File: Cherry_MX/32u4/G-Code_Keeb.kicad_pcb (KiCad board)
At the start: 2 copper layers, 158.7 x 133.3 mm, 46 parts, among them J1 Conn_01x04, SW1 SW_Push_45deg, SW10 SW_Push_45deg, SW11 SW_Push_45deg, SW12 SW_Push_45deg, SW13 SW_Push_45deg, SW14 SW_Push_45deg, SW15 SW_Push_45deg, SW16 SW_Push_45deg, SW17 SW_Push_45deg, SW18 SW_Push_45deg, SW19 SW_Push_45deg, SW2 SW_Push_45deg, SW20 SW_Push_45deg, SW21 SW_Push_45deg, SW22 SW_Push_45deg, SW23 SW_Push_45deg, SW24 SW_Push, SW25 SW_Push, SW3 SW_Push_45deg, SW4 SW_Push_45deg, SW5 SW_Push_45deg, SW6 SW_Push_45deg, SW7 SW_Push_45deg, SW8 SW_Push_45deg, SW9 SW_Push_45deg, U1 ATmega32U4-A, Y1 16MHz

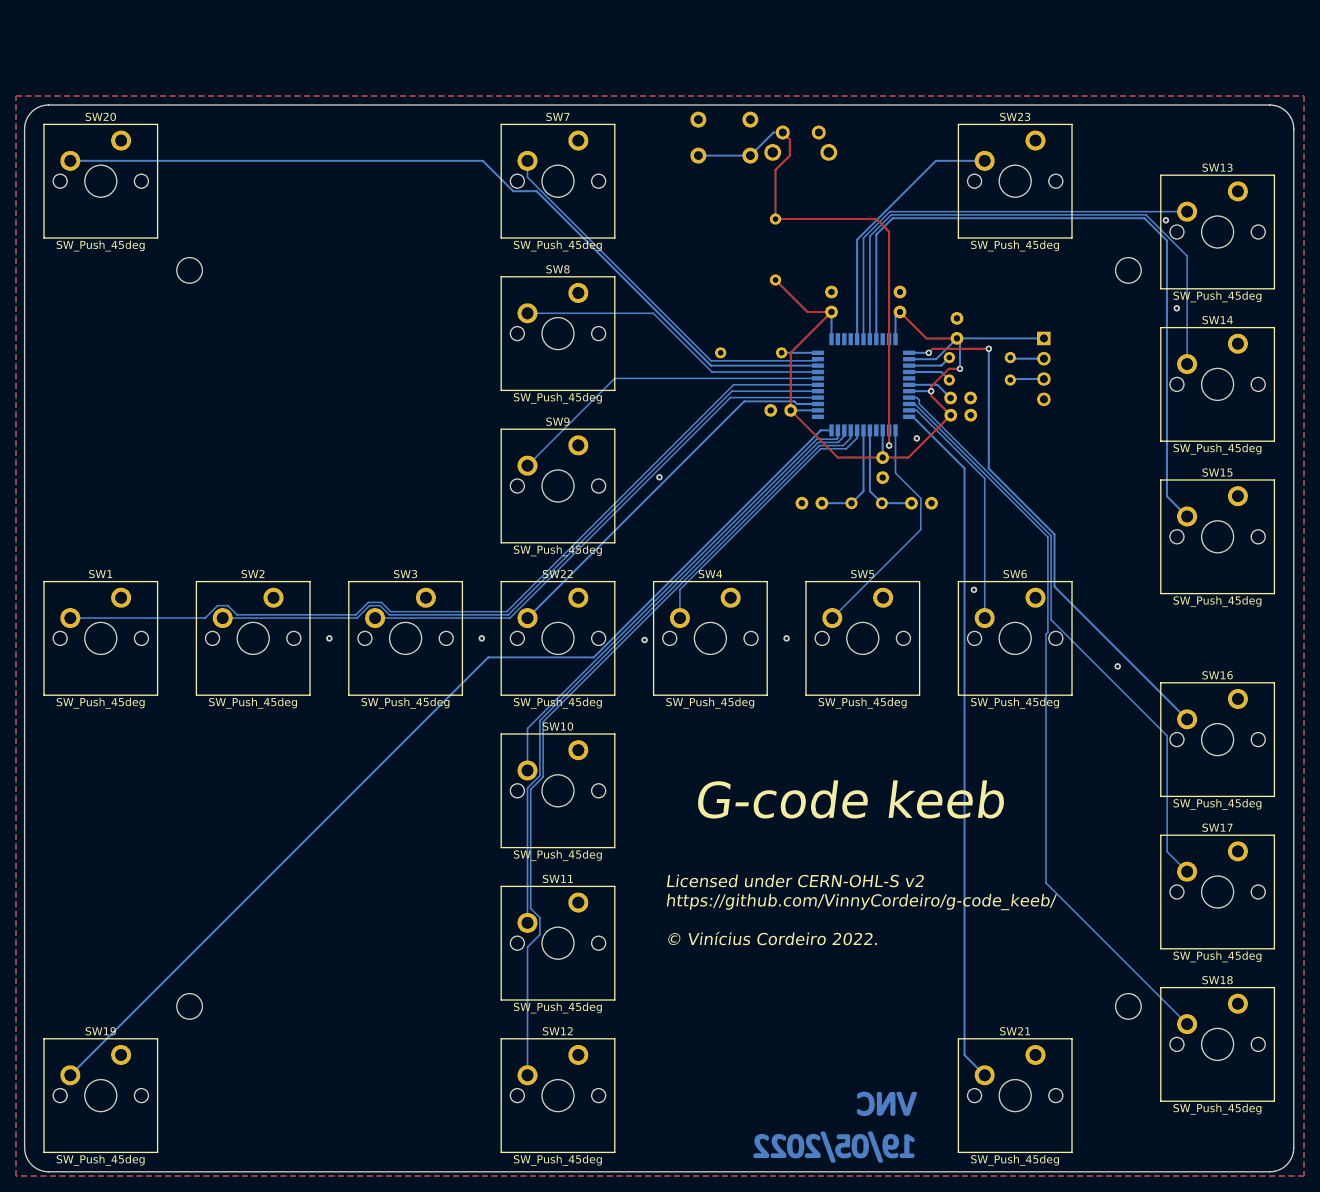
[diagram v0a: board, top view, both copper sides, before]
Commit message: Fixed mistake on X axis
The X axis values were mirrored, this commit fix that. That also includes the silkscreen.
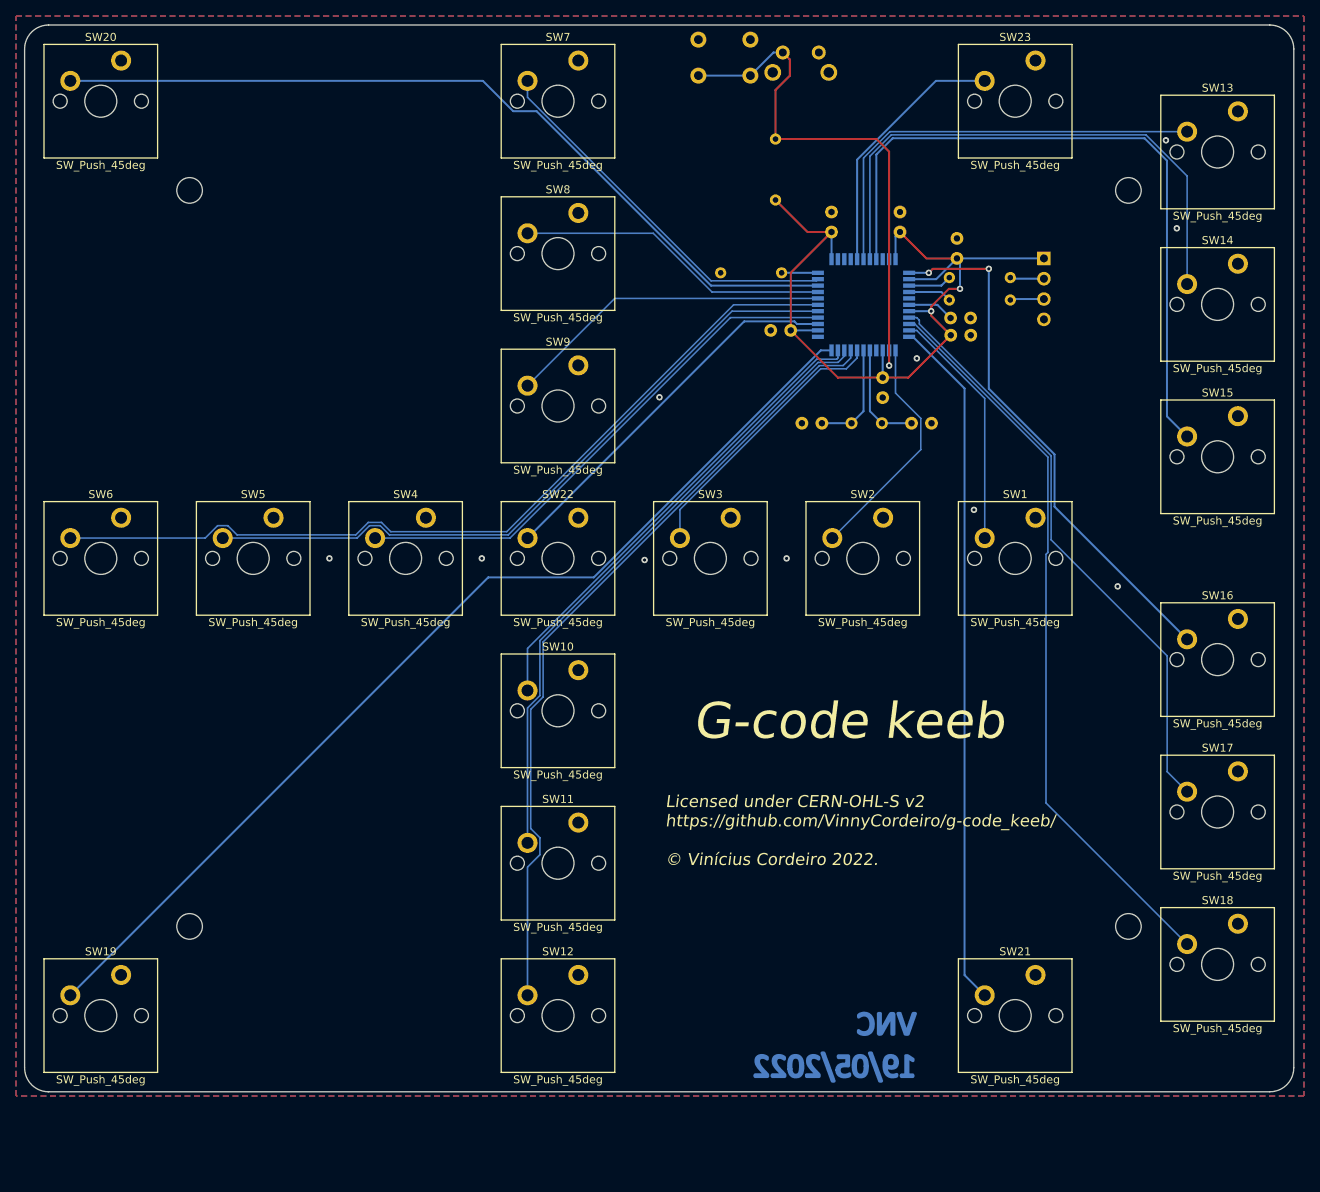
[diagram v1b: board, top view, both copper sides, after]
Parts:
- moved SW1 114.7 mm to (142.9, 94.8)
- moved SW6 114.7 mm to (28.6, 94.8)
- moved SW2 76.9 mm to (123.8, 94.8)
- moved SW5 76.9 mm to (47.6, 94.8)
- moved SW3 39.4 mm to (104.8, 94.8)
- moved SW4 39.4 mm to (66.7, 94.8)
- moved G*** 11.1 mm to (59.1, 94.8)
- moved SW25 10.0 mm to (109.8, 29.9)
- moved C1 10.0 mm to (132.4, 77.9)
- moved C2 10.0 mm to (118.7, 77.9)
- moved C3 10.0 mm to (137.3, 64.8)
- moved C4 10.0 mm to (135.6, 54.8)
- moved C5 10.0 mm to (137.3, 66.9)
- moved C6 10.0 mm to (126.3, 74.7)
- moved C7 10.0 mm to (112.3, 66.3)
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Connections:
- U1 pad 10: X-100 -> X+100
- U1 pad 12: X-10 -> X+10
- U1 pad 18: X-1 -> X+1
- U1 pad 26: X+1 -> X-1
- U1 pad 27: X+10 -> X-10
- U1 pad 28: X+100 -> X-100
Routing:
- net X+100: track 107.4 -> 30.4 mm
- net X-100: track 30.4 -> 107.4 mm
- net X-10: track 29.4 -> 87.1 mm
- net X+10: track 87.1 -> 29.4 mm
- net X-1: track 34.5 -> 66.8 mm
- net X+1: track 66.8 -> 34.5 mm

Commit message: Fixing the fix
Uploaded the wrong files, this commit corrects that.
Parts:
- SW1: value SW_Push_45deg -> Z+100
- SW10: value SW_Push_45deg -> Y-1
- SW11: value SW_Push_45deg -> Y-10
- SW12: value SW_Push_45deg -> Y-100
- SW13, SW2: value SW_Push_45deg -> Z+10
- SW14, SW3: value SW_Push_45deg -> Z+1
- SW15: value SW_Push_45deg -> Z+0.1
- SW16: value SW_Push_45deg -> Z-0.1
- SW17: value SW_Push_45deg -> Z-1
- SW18: value SW_Push_45deg -> Z-10
- SW19: value SW_Push_45deg -> HOME
- SW20: value SW_Push_45deg -> HOME X
- SW21: value SW_Push_45deg -> HOME Y
- SW22: value SW_Push_45deg -> HOME XY
- SW23: value SW_Push_45deg -> HOME Z
- SW4: value SW_Push_45deg -> X-1
- SW5: value SW_Push_45deg -> X-10
- SW6: value SW_Push_45deg -> X-100
- SW7: value SW_Push_45deg -> Y+100
- SW8: value SW_Push_45deg -> Y+10
- SW9: value SW_Push_45deg -> Y+1

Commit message: Fixing silkscreen
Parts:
- SW1: value Z+100 -> X+100
- SW2: value Z+10 -> X+10
- SW3: value Z+1 -> X+1
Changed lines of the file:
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@@
       (effects (font (size 1 1) (thickness 0.15)))
     )
-    (fp_text value "Z+10" (at 0 8) (layer "F.SilkS")
+    (fp_text value "X+10" (at 0 8) (layer "F.SilkS")
       (effects (font (size 1 1) (thickness 0.15)))
     )
@@
       (effects (font (size 1 1) (thickness 0.15)))
     )
-    (fp_text value "Z+100" (at 0 8) (layer "F.SilkS")
+    (fp_text value "X+100" (at 0 8) (layer "F.SilkS")
       (effects (font (size 1 1) (thickness 0.15)))
     )
@@
       (effects (font (size 1 1) (thickness 0.15)))
     )
-    (fp_text value "Z+1" (at 0 8) (layer "F.SilkS")
-      (effects (font (size 1 1) (thickness 0.15)))
-    )
+    (fp_text value "X+1" (at 0 8) (layer "F.SilkS")
+      (effects (font (size 1 1) (thickness 0.15)))
+    )

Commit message: Yet another silkscreen fix
It never ends
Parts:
- removed G***: LOGO, Footprints:table
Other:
- board text added: "--------------- | Function | MCU pin | --------------- | X+1 | PD0 | --------------- | X+10 | PB7 | --------------- | X+100 | PB2 | --------------- | X-1 | PD6 | --------------- | X-10 | PD7 | --------------- | X-100 | PB4 | --------------- | Y+1 | PB5 | --------------- | Y+10 | PB6 | --------------- | Y+100 | PC7 | --------------- | Y-1 | PD3 | --------------- | Y-10 | PD2 | --------------- | Y-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"
